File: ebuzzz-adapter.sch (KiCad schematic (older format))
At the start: 33 parts, among them J1 Conn_01x04, J2 Conn_01x04, J3 Conn_01x06, J4 EBUS, Q1 BC817-40, U1 CNY17-4, U2 CNY17-4, U3 LM2903, U4 LP2951-5.0_SOIC

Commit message: Version 1 release (hardware tested)
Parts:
- added D6: 1N4148WS, Diode_SMD:D_SOD-323, symbol Diode:1N4148WS
- D3: Farnell (none) -> 1611267
- R16: value 10E -> 120E
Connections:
- net +5V: now also R11.1, R9.1; no longer R10.1, R11.2, R12.1, U3.3 (+), U3.5 (+)
- net ebus-signal: now also D6.2 (A); no longer R16.2
- net at R9.2, U3.1, U3.6 (_): now also R10.2
- new net: R10.1, R11.2, R12.1, U3.3 (+), U3.5 (+)
- new net: D6.1 (K), R16.2
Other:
- moved on the sheet: R10, R11, R13, R16, R9
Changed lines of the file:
@@
 L Device:R_Small R11
 U 1 1 5D4C8B84
-P 7100 1250
-F 0 "R11" H 7159 1296 50  0000 L CNN
-F 1 "18k" H 7159 1205 50  0000 L CNN
-F 2 "Resistor_SMD:R_0805_2012Metric_Pad1.15x1.40mm_HandSolder" H 7100 1250 50  0001 C CNN
-F 3 "~" H 7100 1250 50  0001 C CNN
-	1    7100 1250
+P 7100 1100
+F 0 "R11" H 7159 1146 50  0000 L CNN
+F 1 "18k" H 7159 1055 50  0000 L CNN
+F 2 "Resistor_SMD:R_0805_2012Metric_Pad1.15x1.40mm_HandSolder" H 7100 1100 50  0001 C CNN
+F 3 "~" H 7100 1100 50  0001 C CNN
+	1    7100 1100
 	1    0    0    -1
 $EndComp
@@
 L Device:R_Small R13
 U 1 1 5D4C8EDF
-P 7350 1650
-F 0 "R13" H 7409 1696 50  0000 L CNN
-F 1 "100k" H 7409 1605 50  0000 L CNN
-F 2 "Resistor_SMD:R_0805_2012Metric_Pad1.15x1.40mm_HandSolder" H 7350 1650 50  0001 C CNN
-F 3 "~" H 7350 1650 50  0001 C CNN
-	1    7350 1650
+P 7350 1850
+F 0 "R13" H 7409 1896 50  0000 L CNN
+F 1 "100k" H 7409 1805 50  0000 L CNN
+F 2 "Resistor_SMD:R_0805_2012Metric_Pad1.15x1.40mm_HandSolder" H 7350 1850 50  0001 C CNN
+F 3 "~" H 7350 1850 50  0001 C CNN
+	1    7350 1850
 	1    0    0    -1
 $EndComp
@@
 L Device:R_Small R10
 U 1 1 5D4C977A
-P 6850 1450
-F 0 "R10" V 6654 1450 50  0000 C CNN
-F 1 "220k" V 6745 1450 50  0000 C CNN
-F 2 "Resistor_SMD:R_0805_2012Metric_Pad1.15x1.40mm_HandSolder" H 6850 1450 50  0001 C CNN
-F 3 "~" H 6850 1450 50  0001 C CNN
-	1    6850 1450
+P 6700 1300
+F 0 "R10" V 6504 1300 50  0000 C CNN
+F 1 "220k" V 6595 1300 50  0000 C CNN
+F 2 "Resistor_SMD:R_0805_2012Metric_Pad1.15x1.40mm_HandSolder" H 6700 1300 50  0001 C CNN
+F 3 "~" H 6700 1300 50  0001 C CNN
+	1    6700 1300
 	0    1    1    0
 $EndComp
@@
 L Device:R_Small R9
 U 1 1 5D4CA98C
-P 6300 1650
-F 0 "R9" H 6359 1696 50  0000 L CNN
-F 1 "10k" H 6359 1605 50  0000 L CNN
-F 2 "Resistor_SMD:R_0805_2012Metric_Pad1.15x1.40mm_HandSolder" H 6300 1650 50  0001 C CNN
-F 3 "~" H 6300 1650 50  0001 C CNN
-	1    6300 1650
+P 6300 1100
+F 0 "R9" H 6359 1146 50  0000 L CNN
+F 1 "10k" H 6359 1055 50  0000 L CNN
+F 2 "Resistor_SMD:R_0805_2012Metric_Pad1.15x1.40mm_HandSolder" H 6300 1100 50  0001 C CNN
+F 3 "~" H 6300 1100 50  0001 C CNN
+	1    6300 1100
 	1    0    0    -1
 $EndComp
@@
 	7350 2050 7350 2150
 Wire Wire Line
-	7350 1750 7350 2050
+	7350 1950 7350 2050
 Connection ~ 7350 2050
 Wire Wire Line
@@
 Connection ~ 7100 1850
 Wire Wire Line
-	7100 1350 7100 1450
-Wire Wire Line
-	6950 1450 7100 1450
-Connection ~ 7100 1450
-Wire Wire Line
-	7100 1450 7100 1850
-Wire Wire Line
-	7100 1150 6300 1150
-Wire Wire Line
-	6300 1150 6300 1450
-Wire Wire Line
-	6300 1450 6750 1450
-Wire Wire Line
-	6300 1450 6300 1550
-Connection ~ 6300 1450
-Wire Wire Line
-	6300 1750 6300 1950
+	7100 1200 7100 1300
+Wire Wire Line
+	6800 1300 7100 1300
+Connection ~ 7100 1300
+Wire Wire Line
+	6300 950  6300 1000
+Wire Wire Line
+	6300 1300 6600 1300
+Connection ~ 6300 1300
 Wire Wire Line
 	6300 1950 6400 1950
 Wire Wire Line
 	6000 1750 6150 1750
-Wire Wire Line
-	6150 1050 7300 1050
-Wire Wire Line
-	7300 1050 7300 1450
-Wire Wire Line
-	7300 1450 7100 1450
-Wire Wire Line
-	6150 1050 6150 1750
 Wire Wire Line
 	6000 1950 6300 1950
@@
 Wire Wire Line
 	9150 3250 9150 3000
-$Comp
-L power:+5V #PWR05
-U 1 1 5D516E86
-P 6150 950
-F 0 "#PWR05" H 6150 800 50  0001 C CNN
-F 1 "+5V" H 6165 1123 50  0000 C CNN
-F 2 "" H 6150 950 50  0001 C CNN
-F 3 "" H 6150 950 50  0001 C CNN
-	1    6150 950
-	1    0    0    -1
-$EndComp
-Wire Wire Line
-	6150 950  6150 1050
-Connection ~ 6150 1050
 $Comp
 L power:+5V #PWR01
@@
 	8600 2650 7700 2650
 Wire Wire Line
-	7700 2650 7700 1500
-Wire Wire Line
-	7700 1500 7350 1500
-Wire Wire Line
-	7350 1500 7350 1550
+	7700 2650 7700 1700
+Wire Wire Line
+	7700 1700 7350 1700
+Wire Wire Line
+	7350 1700 7350 1750
 $Comp
 L power:0V #PWR010
@@
 	8000 1250 8000 1350
 Wire Wire Line
-	7700 1050 7700 1200
-Connection ~ 7700 1500
+	7700 1050 7700 1150
 Wire Wire Line
 	7700 1050 7800 1050
@@
 F 2 "Diode_SMD:D_SMA" H 6200 2475 50  0001 C CNN
 F 3 "https://diotec.com/tl_files/diotec/files/pdf/datasheets/z1sma1.pdf" H 6200 2650 50  0001 C CNN
+F 4 "1611267" H 6200 2650 50  0001 C CNN "Farnell"
 	1    6200 2650
 	-1   0    0    1
@@
 L Device:R_Small R16
 U 1 1 5D77CA1D
-P 7700 1300
-F 0 "R16" H 7759 1346 50  0000 L CNN
-F 1 "10E" H 7759 1255 50  0000 L CNN
-F 2 "Resistor_SMD:R_0805_2012Metric_Pad1.15x1.40mm_HandSolder" H 7700 1300 50  0001 C CNN
-F 3 "~" H 7700 1300 50  0001 C CNN
-	1    7700 1300
+P 7700 1250
+F 0 "R16" H 7759 1296 50  0000 L CNN
+F 1 "120E" H 7759 1205 50  0000 L CNN
+F 2 "Resistor_SMD:R_0805_2012Metric_Pad1.15x1.40mm_HandSolder" H 7700 1250 50  0001 C CNN
+F 3 "~" H 7700 1250 50  0001 C CNN
+	1    7700 1250
 	-1   0    0    -1
 $EndComp
-Wire Wire Line
-	7700 1400 7700 1500
-$Comp
-L power:0V #PWR?
+$Comp
+L power:0V #PWR0101
 U 1 1 5D521163
 P 5700 3450
-F 0 "#PWR?" H 5700 3200 50  0001 C CNN
+F 0 "#PWR0101" H 5700 3200 50  0001 C CNN
 F 1 "0V" H 5705 3277 50  0000 C CNN
 F 2 "" H 5700 3450 50  0001 C CNN
@@
 	1    0    0    -1
 $EndComp
+Wire Wire Line
+	7100 950  7100 1000
+$Comp
+L power:+5V #PWR04
+U 1 1 5D5B09A3
+P 6300 950
+F 0 "#PWR04" H 6300 800 50  0001 C CNN
+F 1 "+5V" H 6315 1123 50  0000 C CNN
+F 2 "" H 6300 950 50  0001 C CNN
+F 3 "" H 6300 950 50  0001 C CNN
+	1    6300 950
+	1    0    0    -1
+$EndComp
+Wire Wire Line
+	6150 1450 6150 1750
+Wire Wire Line
+	7100 1450 7100 1850
+Connection ~ 7100 1450
+Wire Wire Line
+	7100 1300 7100 1450
+Wire Wire Line
+	7100 1450 6150 1450
+$Comp
+L power:+5V #PWR05
+U 1 1 5D516E86
+P 7100 950
+F 0 "#PWR05" H 7100 800 50  0001 C CNN
+F 1 "+5V" H 7115 1123 50  0000 C CNN
+F 2 "" H 7100 950 50  0001 C CNN
+F 3 "" H 7100 950 50  0001 C CNN
+	1    7100 950
+	1    0    0    -1
+$EndComp
+Wire Wire Line
+	6300 1200 6300 1300
+Wire Wire Line
+	6300 1300 6300 1950
+$Comp
+L Diode:1N4148WS D6
+U 1 1 5DACF05D
+P 7700 1550
+F 0 "D6" V 7650 1100 50  0000 L CNN
+F 1 "1N4148WS" V 7750 1100 50  0000 L CNN
+F 2 "Diode_SMD:D_SOD-323" H 7700 1375 50  0001 C CNN
+F 3 "https://www.vishay.com/docs/85751/1n4148ws.pdf" H 7700 1550 50  0001 C CNN
+F 4 "2675148" V 7700 1550 50  0001 C CNN "Farnell"
+	1    7700 1550
+	0    1    1    0
+$EndComp
+Connection ~ 7700 1700
+Wire Wire Line
+	7700 1350 7700 1400
 $EndSCHEMATC

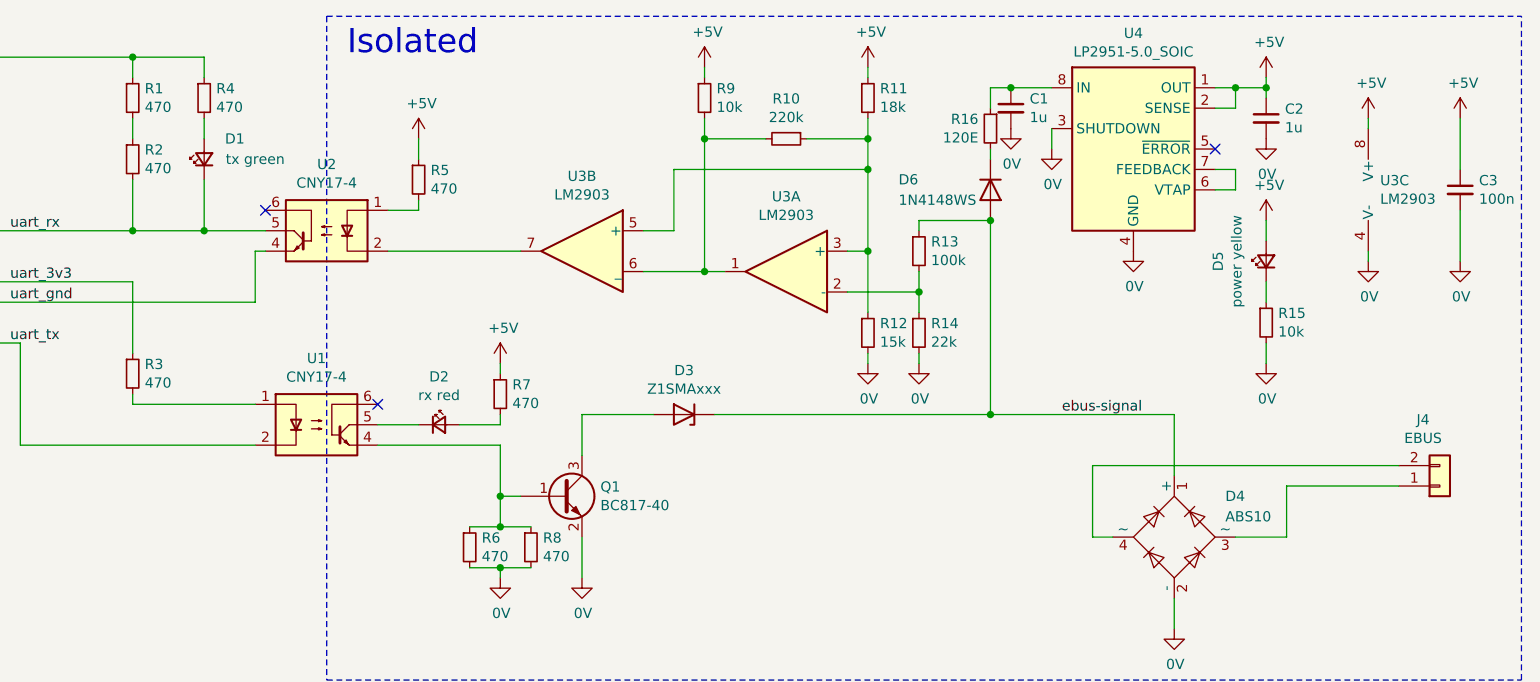
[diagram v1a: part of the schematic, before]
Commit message: added LCSC components (and tuned values)
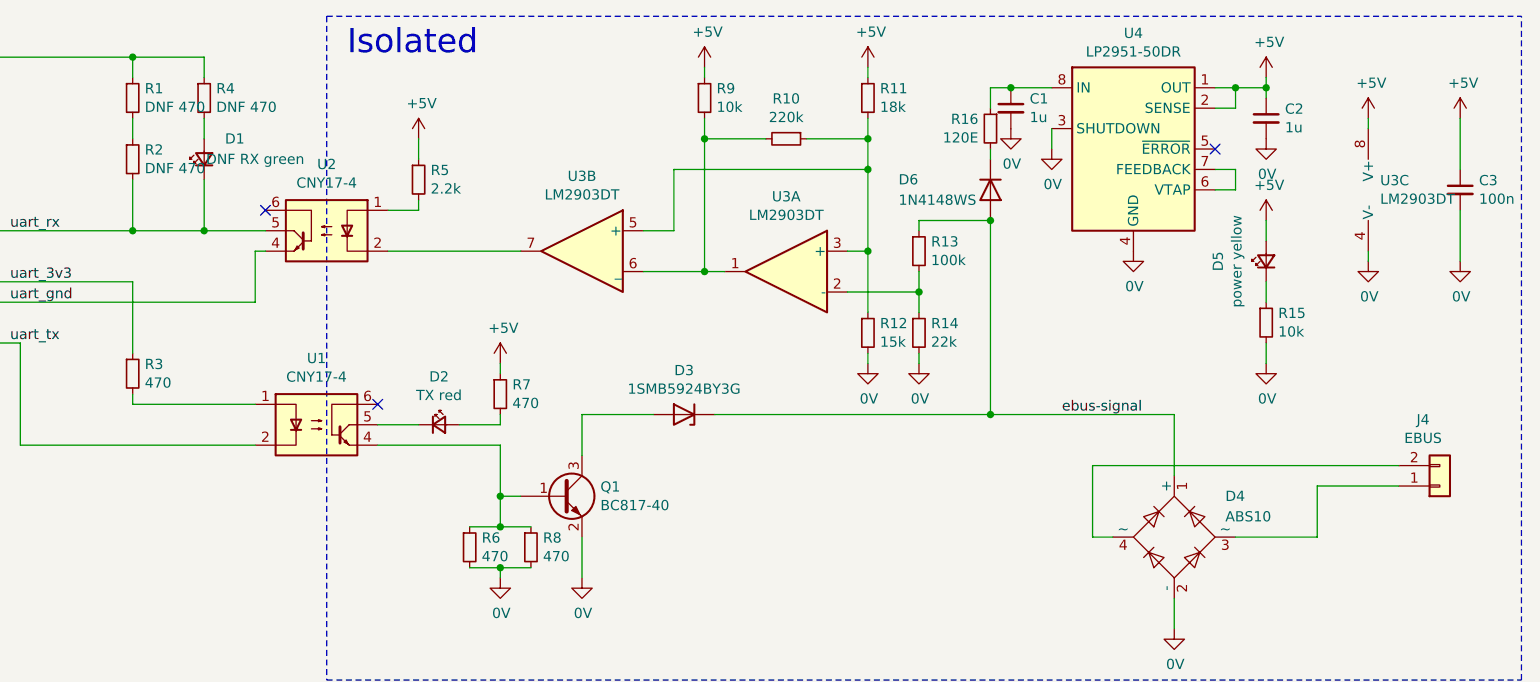
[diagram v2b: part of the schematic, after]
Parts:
- C1, C2: LCSC (none) -> C28323
- C3: LCSC (none) -> C49678
- D1: value tx green -> DNF RX green
- D2: value rx red -> TX red; LCSC (none) -> C84256
- D3: value Z1SMAxxx -> 1SMB5924BY3G; LCSC (none) -> C53166
- D4: LCSC (none) -> C65028
- D5: LCSC (none) -> C2296
- D6: LCSC (none) -> C57759
- Q1: LCSC (none) -> C181151
- R1, R2, R4: value 470 -> DNF 470
- R10: LCSC (none) -> C17556
- R11: LCSC (none) -> C17506
- R12, R14: LCSC (none) -> C17475
- R13: LCSC (none) -> C17407
- R15, R9: LCSC (none) -> C17414
- R16: LCSC (none) -> C17437
- R3, R6, R7, R8: LCSC (none) -> C17710
- R5: value 470 -> 2.2k; LCSC (none) -> C17520
- U3: value LM2903 -> LM2903DT; LCSC (none) -> C98194
- U3: value LM2903 -> LM2903DT
- U4: value LP2951-5.0_SOIC -> LP2951-50DR; LCSC (none) -> C109380
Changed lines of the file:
@@
 EESchema Schematic File Version 4
-LIBS:ebuzzz-adapter-cache
 EELAYER 30 0
 EELAYER END
@@
 F 3 "https://diotec.com/tl_files/diotec/files/pdf/datasheets/abs2.pdf" H 8600 3250 50  0001 C CNN
 F 4 "3127182" V 8600 3250 50  0001 C CNN "Farnell"
+F 5 "C65028" V 8600 3250 50  0001 C CNN "LCSC"
 	1    8600 3250
 	0    -1   -1   0
 $EndComp
 Wire Wire Line
-	9700 3000 9150 3000
+	9700 3000 9300 3000
 Wire Wire Line
 	9700 2900 8200 2900
@@
 P 6700 1950
 F 0 "U3" H 6700 2317 50  0000 C CNN
-F 1 "LM2903" H 6700 2226 50  0000 C CNN
+F 1 "LM2903DT" H 6700 2226 50  0000 C CNN
 F 2 "Package_SO:SOIC-8_3.9x4.9mm_P1.27mm" H 6700 1950 50  0001 C CNN
 F 3 "http://www.ti.com/lit/ds/symlink/lm393-n.pdf" H 6700 1950 50  0001 C CNN
 F 4 "2382615" H 6700 1950 50  0001 C CNN "Farnell"
+F 5 "C98194" H 6700 1950 50  0001 C CNN "LCSC"
 	1    6700 1950
 	-1   0    0    -1
@@
 P 5700 1850
 F 0 "U3" H 5700 2217 50  0000 C CNN
-F 1 "LM2903" H 5700 2126 50  0000 C CNN
+F 1 "LM2903DT" H 5700 2126 50  0000 C CNN
 F 2 "Package_SO:SOIC-8_3.9x4.9mm_P1.27mm" H 5700 1850 50  0001 C CNN
 F 3 "http://www.ti.com/lit/ds/symlink/lm393-n.pdf" H 5700 1850 50  0001 C CNN
@@
 P 9650 1550
 F 0 "U3" H 9608 1596 50  0000 L CNN
-F 1 "LM2903" H 9608 1505 50  0000 L CNN
+F 1 "LM2903DT" H 9608 1505 50  0000 L CNN
 F 2 "Package_SO:SOIC-8_3.9x4.9mm_P1.27mm" H 9650 1550 50  0001 C CNN
 F 3 "http://www.ti.com/lit/ds/symlink/lm393-n.pdf" H 9650 1550 50  0001 C CNN
@@
 F 2 "Resistor_SMD:R_0805_2012Metric_Pad1.15x1.40mm_HandSolder" H 7350 2250 50  0001 C CNN
 F 3 "~" H 7350 2250 50  0001 C CNN
+F 4 "C17475" H 7350 2250 50  0001 C CNN "LCSC"
 	1    7350 2250
 	1    0    0    -1
@@
 F 2 "Resistor_SMD:R_0805_2012Metric_Pad1.15x1.40mm_HandSolder" H 7100 2250 50  0001 C CNN
 F 3 "~" H 7100 2250 50  0001 C CNN
+F 4 "C17475" H 7100 2250 50  0001 C CNN "LCSC"
 	1    7100 2250
 	1    0    0    -1
@@
 F 2 "Resistor_SMD:R_0805_2012Metric_Pad1.15x1.40mm_HandSolder" H 7100 1100 50  0001 C CNN
 F 3 "~" H 7100 1100 50  0001 C CNN
+F 4 "C17506" H 7100 1100 50  0001 C CNN "LCSC"
 	1    7100 1100
 	1    0    0    -1
@@
 F 2 "Resistor_SMD:R_0805_2012Metric_Pad1.15x1.40mm_HandSolder" H 7350 1850 50  0001 C CNN
 F 3 "~" H 7350 1850 50  0001 C CNN
+F 4 "C17407" H 7350 1850 50  0001 C CNN "LCSC"
 	1    7350 1850
 	1    0    0    -1
@@
 F 2 "Resistor_SMD:R_0805_2012Metric_Pad1.15x1.40mm_HandSolder" H 6700 1300 50  0001 C CNN
 F 3 "~" H 6700 1300 50  0001 C CNN
+F 4 "C17556" V 6700 1300 50  0001 C CNN "LCSC"
 	1    6700 1300
 	0    1    1    0
@@
 F 2 "Resistor_SMD:R_0805_2012Metric_Pad1.15x1.40mm_HandSolder" H 6300 1100 50  0001 C CNN
 F 3 "~" H 6300 1100 50  0001 C CNN
+F 4 "C17414" H 6300 1100 50  0001 C CNN "LCSC"
 	1    6300 1100
 	1    0    0    -1
@@
 P 4900 1500
 F 0 "R5" H 4959 1546 50  0000 L CNN
-F 1 "470" H 4959 1455 50  0000 L CNN
+F 1 "2.2k" H 4959 1455 50  0000 L CNN
 F 2 "Resistor_SMD:R_0805_2012Metric_Pad1.15x1.40mm_HandSolder" H 4900 1500 50  0001 C CNN
 F 3 "~" H 4900 1500 50  0001 C CNN
+F 4 "C17520" H 4900 1500 50  0001 C CNN "LCSC"
 	1    4900 1500
 	1    0    0    -1
@@
 Isolated
 Wire Wire Line
-	8900 3250 9150 3250
-Wire Wire Line
-	9150 3250 9150 3000
+	8900 3250 9300 3250
+Wire Wire Line
+	9300 3250 9300 3000
 $Comp
 L power:+5V #PWR01
@@
 P 8400 1350
 F 0 "U4" H 8400 1917 50  0000 C CNN
-F 1 "LP2951-5.0_SOIC" H 8400 1826 50  0000 C CNN
+F 1 "LP2951-50DR" H 8400 1826 50  0000 C CNN
 F 2 "Package_SO:SOIC-8_3.9x4.9mm_P1.27mm" H 8400 700 50  0001 C CNN
 F 3 "http://www.ti.com/lit/ds/symlink/lp2951-n.pdf" H 8400 1350 50  0001 C CNN
 F 4 "1755065" H 8400 1350 50  0001 C CNN "Farnell"
+F 5 "C109380" H 8400 1350 50  0001 C CNN "LCSC"
 	1    8400 1350
 	1    0    0    -1
@@
 F 2 "Capacitor_SMD:C_0805_2012Metric_Pad1.15x1.40mm_HandSolder" H 7800 1150 50  0001 C CNN
 F 3 "~" H 7800 1150 50  0001 C CNN
+F 4 "C28323" H 7800 1150 50  0001 C CNN "LCSC"
 	1    7800 1150
 	1    0    0    -1
@@
 F 2 "Capacitor_SMD:C_0805_2012Metric_Pad1.15x1.40mm_HandSolder" H 9050 1200 50  0001 C CNN
 F 3 "~" H 9050 1200 50  0001 C CNN
+F 4 "C28323" H 9050 1200 50  0001 C CNN "LCSC"
 	1    9050 1200
 	1    0    0    -1
@@
 P 5000 2700
 F 0 "D2" H 5000 2935 50  0000 C CNN
-F 1 "rx red" H 5000 2844 50  0000 C CNN
+F 1 "TX red" H 5000 2844 50  0000 C CNN
 F 2 "LED_SMD:LED_0805_2012Metric_Pad1.15x1.40mm_HandSolder" V 5000 2700 50  0001 C CNN
 F 3 "~" V 5000 2700 50  0001 C CNN
+F 4 "C84256" H 5000 2700 50  0001 C CNN "LCSC"
 	1    5000 2700
 	1    0    0    -1
@@
 F 2 "Resistor_SMD:R_0805_2012Metric_Pad1.15x1.40mm_HandSolder" H 5300 2550 50  0001 C CNN
 F 3 "~" H 5300 2550 50  0001 C CNN
+F 4 "C17710" H 5300 2550 50  0001 C CNN "LCSC"
 	1    5300 2550
 	1    0    0    -1
@@
 F 3 "http://www.fairchildsemi.com/ds/BC/BC817.pdf" H 5600 3050 50  0001 L CNN
 F 4 "1798081" H 5600 3050 50  0001 C CNN "Farnell"
+F 5 "C181151" H 5600 3050 50  0001 C CNN "LCSC"
 	1    5600 3050
 	1    0    0    -1
@@
 P 6200 2650
 F 0 "D3" H 6200 2434 50  0000 C CNN
-F 1 "Z1SMAxxx" H 6200 2525 50  0000 C CNN
+F 1 "1SMB5924BY3G" H 6200 2525 50  0000 C CNN
 F 2 "Diode_SMD:D_SMA" H 6200 2475 50  0001 C CNN
 F 3 "https://diotec.com/tl_files/diotec/files/pdf/datasheets/z1sma1.pdf" H 6200 2650 50  0001 C CNN
 F 4 "1611267" H 6200 2650 50  0001 C CNN "Farnell"
+F 5 "C53166" H 6200 2650 50  0001 C CNN "LCSC"
 	1    6200 2650
 	-1   0    0    1
@@
 P 3850 1400
 F 0 "D1" V 3950 1250 50  0000 C CNN
-F 1 "tx green" V 3850 1150 50  0000 C CNN
+F 1 "DNF RX green" V 3850 1150 50  0000 C CNN
 F 2 "LED_SMD:LED_0805_2012Metric_Pad1.15x1.40mm_HandSolder" V 3850 1400 50  0001 C CNN
 F 3 "~" V 3850 1400 50  0001 C CNN
@@
 P 3850 1100
 F 0 "R4" H 3909 1146 50  0000 L CNN
-F 1 "470" H 3909 1055 50  0000 L CNN
+F 1 "DNF 470" H 3909 1055 50  0000 L CNN
 F 2 "Resistor_SMD:R_0805_2012Metric_Pad1.15x1.40mm_HandSolder" H 3850 1100 50  0001 C CNN
 F 3 "~" H 3850 1100 50  0001 C CNN
@@
 P 3500 1100
 F 0 "R1" H 3559 1146 50  0000 L CNN
-F 1 "470" H 3559 1055 50  0000 L CNN
+F 1 "DNF 470" H 3559 1055 50  0000 L CNN
 F 2 "Resistor_SMD:R_0805_2012Metric_Pad1.15x1.40mm_HandSolder" H 3500 1100 50  0001 C CNN
 F 3 "~" H 3500 1100 50  0001 C CNN
@@
 P 3500 1400
 F 0 "R2" H 3559 1446 50  0000 L CNN
-F 1 "470" H 3559 1355 50  0000 L CNN
+F 1 "DNF 470" H 3559 1355 50  0000 L CNN
 F 2 "Resistor_SMD:R_0805_2012Metric_Pad1.15x1.40mm_HandSolder" H 3500 1400 50  0001 C CNN
 F 3 "~" H 3500 1400 50  0001 C CNN
@@
 F 2 "Resistor_SMD:R_0805_2012Metric_Pad1.15x1.40mm_HandSolder" H 3500 2450 50  0001 C CNN
 F 3 "~" H 3500 2450 50  0001 C CNN
+F 4 "C17710" H 3500 2450 50  0001 C CNN "LCSC"
 	1    3500 2450
 	1    0    0    -1
@@
 F 2 "Resistor_SMD:R_0805_2012Metric_Pad1.15x1.40mm_HandSolder" H 5450 3300 50  0001 C CNN
 F 3 "~" H 5450 3300 50  0001 C CNN
+F 4 "C17710" H 5450 3300 50  0001 C CNN "LCSC"
 	1    5450 3300
 	1    0    0    -1
@@
 F 2 "Resistor_SMD:R_0805_2012Metric_Pad1.15x1.40mm_HandSolder" H 5150 3300 50  0001 C CNN
 F 3 "~" H 5150 3300 50  0001 C CNN
+F 4 "C17710" H 5150 3300 50  0001 C CNN "LCSC"
 	1    5150 3300
 	1    0    0    -1
@@
 F 2 "Capacitor_SMD:C_0805_2012Metric_Pad1.15x1.40mm_HandSolder" H 10000 1550 50  0001 C CNN
 F 3 "~" H 10000 1550 50  0001 C CNN
+F 4 "C49678" H 10000 1550 50  0001 C CNN "LCSC"
 	1    10000 1550
 	1    0    0    -1
@@
 F 2 "LED_SMD:LED_0805_2012Metric_Pad1.15x1.40mm_HandSolder" V 9050 1900 50  0001 C CNN
 F 3 "~" V 9050 1900 50  0001 C CNN
+F 4 "C2296" H 9050 1900 50  0001 C CNN "LCSC"
 	1    9050 1900
 	0    -1   -1   0
@@
 F 2 "Resistor_SMD:R_0805_2012Metric_Pad1.15x1.40mm_HandSolder" H 9050 2200 50  0001 C CNN
 F 3 "~" H 9050 2200 50  0001 C CNN
+F 4 "C17414" H 9050 2200 50  0001 C CNN "LCSC"
 	1    9050 2200
 	1    0    0    -1
@@
 F 2 "Resistor_SMD:R_0805_2012Metric_Pad1.15x1.40mm_HandSolder" H 7700 1250 50  0001 C CNN
 F 3 "~" H 7700 1250 50  0001 C CNN
+F 4 "C17437" H 7700 1250 50  0001 C CNN "LCSC"
 	1    7700 1250
 	-1   0    0    -1
@@
 F 3 "https://www.vishay.com/docs/85751/1n4148ws.pdf" H 7700 1550 50  0001 C CNN
 F 4 "2675148" V 7700 1550 50  0001 C CNN "Farnell"
+F 5 "C57759" V 7700 1550 50  0001 C CNN "LCSC"
 	1    7700 1550
 	0    1    1    0
